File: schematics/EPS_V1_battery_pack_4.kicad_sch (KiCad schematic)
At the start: 31 parts, among them U12 MP2672AGD-0000-Z, U13 MAX17205G+

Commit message: Fix NC pins, add 2 test points & silkscreen labels
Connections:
- net GND: now also U12.14 (SCL), U12.15 (SDA), U13.10 (AIN2), U13.9 (AIN1)
- no-connect marks 6 -> 2
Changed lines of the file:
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@@
+	)
+	(junction
+		(at 104.14 90.17)
+		(diameter 0)
+		(color 0 0 0 0)
 	)
 	(junction
@@
 	)
 	(junction
+		(at 229.87 88.9)
+		(diameter 0)
+		(color 0 0 0 0)
+	)
+	(junction
 		(at 257.81 83.82)
 		(diameter 0)
@@
 	)
 	(junction
+		(at 104.14 92.71)
+		(diameter 0)
+		(color 0 0 0 0)
+	)
+	(junction
 		(at 118.11 105.41)
 		(diameter 0)
@@
 	)
 	(no_connect
-		(at 104.14 90.17)
-	)
-	(no_connect
 		(at 229.87 78.74)
-	)
-	(no_connect
-		(at 229.87 91.44)
 	)
 	(no_connect
 		(at 104.14 95.25)
 	)
-	(no_connect
-		(at 104.14 87.63)
-	)
-	(no_connect
-		(at 229.87 88.9)
-	)
 	(wire
 		(pts
@@
 	(wire
 		(pts
+			(xy 229.87 96.52) (xy 229.87 93.98)
+		)
+		(stroke
+			(width 0)
+			(type default)
+		)
+	)
+	(wire
+		(pts
 			(xy 160.02 78.74) (xy 184.15 78.74)
 		)
@@
 	(wire
 		(pts
-			(xy 229.87 93.98) (xy 231.14 93.98)
+			(xy 229.87 96.52) (xy 232.41 96.52)
 		)
 		(stroke
@@
 	(wire
 		(pts
+			(xy 104.14 90.17) (xy 104.14 92.71)
+		)
+		(stroke
+			(width 0)
+			(type default)
+		)
+	)
+	(wire
+		(pts
 			(xy 114.3 64.77) (xy 48.26 64.77)
 		)
@@
 	(wire
 		(pts
+			(xy 229.87 88.9) (xy 229.87 91.44)
+		)
+		(stroke
+			(width 0)
+			(type default)
+		)
+	)
+	(wire
+		(pts
 			(xy 181.61 83.82) (xy 181.61 102.87)
 		)
@@
 	(wire
 		(pts
+			(xy 104.14 87.63) (xy 104.14 90.17)
+		)
+		(stroke
+			(width 0)
+			(type default)
+		)
+	)
+	(wire
+		(pts
 			(xy 63.5 97.79) (xy 50.8 97.79)
 		)
@@
 		(pts
 			(xy 100.33 107.95) (xy 100.33 120.65)
+		)
+		(stroke
+			(width 0)
+			(type default)
+		)
+	)
+	(wire
+		(pts
+			(xy 229.87 88.9) (xy 233.68 88.9)
 		)
 		(stroke
@@
 	(global_label "ALRT"
 		(shape output)
-		(at 231.14 93.98 0)
+		(at 232.41 96.52 0)
 		(fields_autoplaced yes)
 		(effects
@@
 		)
 		(property "Intersheetrefs" "${INTERSHEET_REFS}"
-			(at 238.4795 93.98 0)
+			(at 239.7495 96.52 0)
 			(hide yes)
 			(show_name no)
@@
 					(unit 1)
 				)
+			)
+		)
+	)
+	(symbol
+		(lib_id "power:GND")
+		(at 233.68 88.9 0)
+		(unit 1)
+		(body_style 1)
+		(exclude_from_sim no)
+		(in_bom yes)
+		(on_board yes)
+		(in_pos_files yes)
+		(dnp no)
+		(property "Reference" "#PWR0129"
+			(at 233.68 95.25 0)
+			(hide yes)
+			(show_name no)
+			(do_not_autoplace no)
+			(effects
+				(font
+					(size 1.27 1.27)
+				)
+			)
+		)
+		(property "Value" "GND"
+			(at 233.68 92.964 0)
+			(show_name no)
+			(do_not_autoplace no)
+			(effects
+				(font
+					(size 1.27 1.27)
+				)
+			)
+		)
+		(property "Footprint" ""
+			(at 233.68 88.9 0)
+			(hide yes)
+			(show_name no)
+			(do_not_autoplace no)
+			(effects
+				(font
+					(size 1.27 1.27)
+				)
+			)
+		)
+		(property "Datasheet" ""
+			(at 233.68 88.9 0)
+			(hide yes)
+			(show_name no)
+			(do_not_autoplace no)
+			(effects
+				(font
+					(size 1.27 1.27)
+				)
+			)
+		)
+		(property "Description" "Power symbol creates a global label with name \"GND\" , ground"
+			(at 233.68 88.9 0)
+			(hide yes)
+			(show_name no)
+			(do_not_autoplace no)
+			(effects
+				(font
+					(size 1.27 1.27)
+				)
+			)
+		)
+		(pin "1"
+		)
+		(instances
+			(project "EPS_V1"
+				(path "/85157432-5d03-48fa-ab40-27ed3d133f47/5659a67b-3108-4102-8b7c-09d96e8fb3f7"
+					(reference "#PWR0129")
+					(unit 1)
+				)

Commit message: Fix silkscreen; Fix component value style
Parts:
- C_BATT8, C_BST4: value 0.1u -> 100n
- C_REG8, C_REG9: value 0.47u -> 470n
- R_BATT4, R_MID4: value 50 -> 50R
- R_SCL4, R_SDA4: value 150 -> 150R
- R_SENSE4: value 0.01 -> 10m
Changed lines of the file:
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@@
 			)
 		)
-		(property "Value" "0.01"
+		(property "Value" "10m"
 			(at 201.676 108.204 90)
 			(show_name no)
@@
 			)
 		)
-		(property "Value" "50"
+		(property "Value" "50R"
 			(at 165.354 81.534 90)
 			(show_name no)
@@
 			)
 		)
-		(property "Value" "0.1u"
+		(property "Value" "100n"
 			(at 167.132 88.9 0)
 			(show_name no)
@@
 			)
 		)
-		(property "Value" "0.47u"
+		(property "Value" "470n"
 			(at 172.212 101.6 0)
 			(show_name no)
@@
 			)
 		)
-		(property "Value" "150"
+		(property "Value" "150R"
 			(at 247.904 91.186 90)
 			(show_name no)
@@
 			)
 		)
-		(property "Value" "50"
+		(property "Value" "50R"
 			(at 61.722 102.87 0)
 			(show_name no)
@@
 			)
 		)
-		(property "Value" "0.47u"
+		(property "Value" "470n"
 			(at 182.118 116.84 0)
 			(show_name no)
@@
 			)
 		)
-		(property "Value" "150"
+		(property "Value" "150R"
 			(at 263.144 78.994 90)
 			(show_name no)
@@
 			)
 		)
-		(property "Value" "0.1u"
+		(property "Value" "100n"
 			(at 55.118 80.01 0)
 			(show_name no)

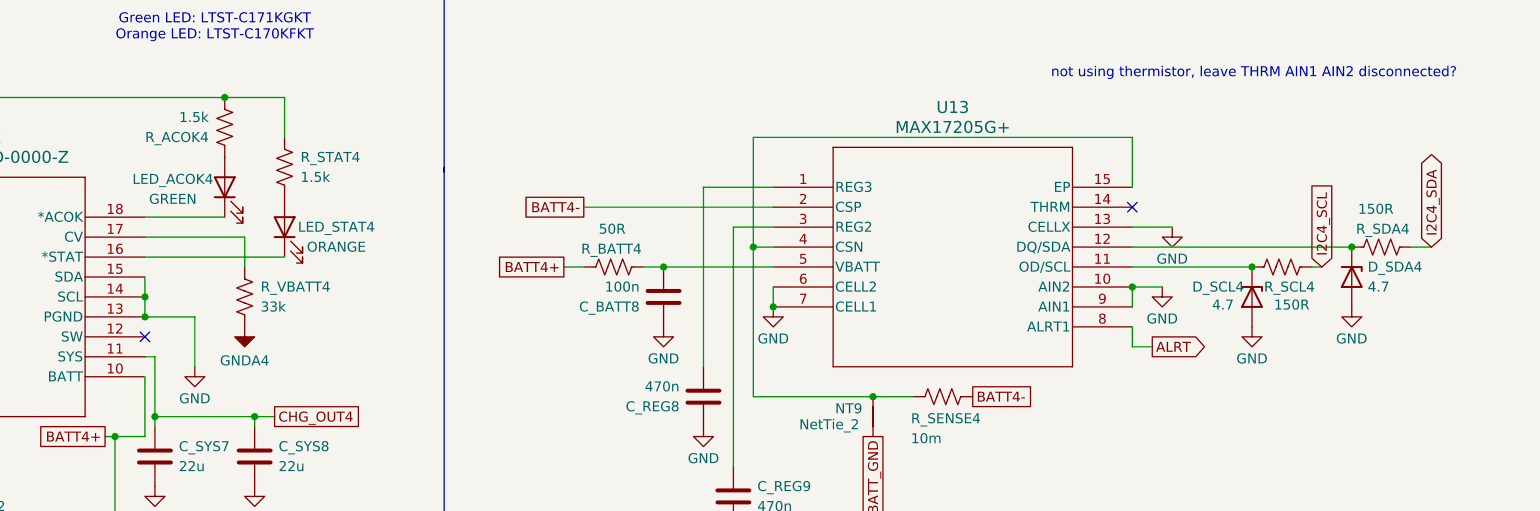
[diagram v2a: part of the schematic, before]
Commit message: Add chargers to I2C, chg_in for ADC
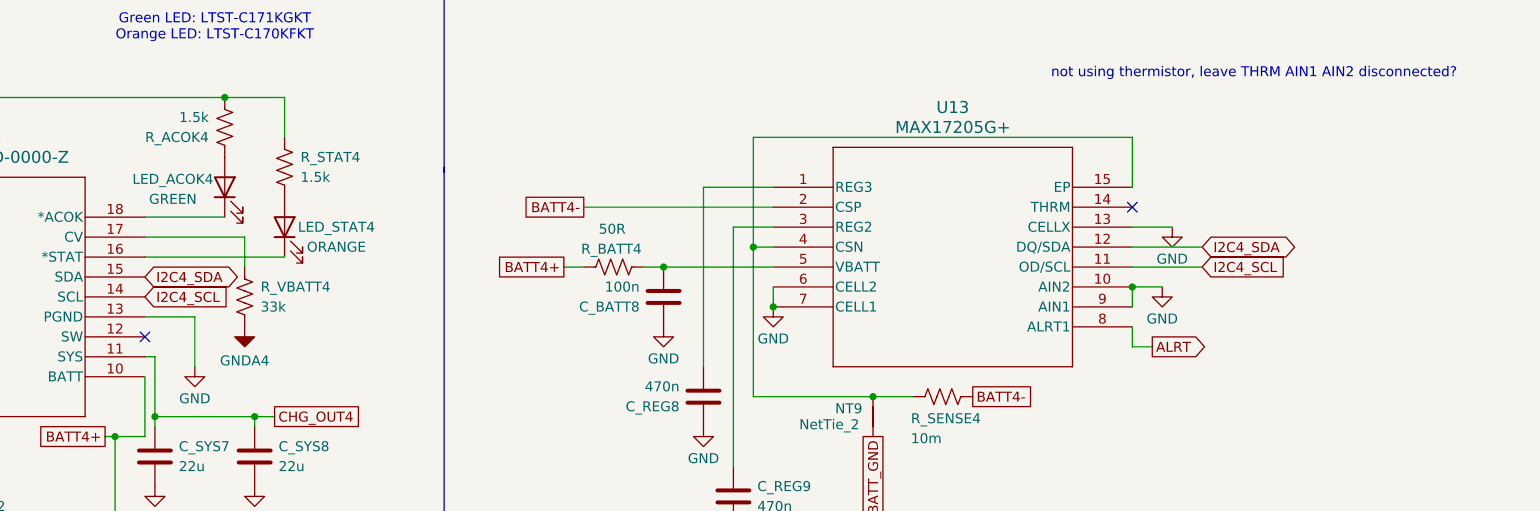
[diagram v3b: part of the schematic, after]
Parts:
- removed D_SCL4, D_SDA4: 4.7, Diode_SMD:D_0603_1608Metric, symbol Device:D_Zener
- removed R_SCL4, R_SDA4: 150R, Resistor_SMD:R_0603_1608Metric, symbol Device:R_US
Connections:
- net GND: no longer U12.14 (SCL), U12.15 (SDA)
- net I2C4_SCL: now also U12.14 (SCL), U13.11 (OD/SCL)
- net I2C4_SDA: now also U12.15 (SDA), U13.12 (DQ/SDA)

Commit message: Fix standalone to host control mode
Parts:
- removed R_VBATT4: 33k, Resistor_SMD:R_0603_1608Metric, symbol Device:R_US
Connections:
- net at C_VCC4.2, R_ACOK4.2, R_STAT4.1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: now also U12.17 (CV)
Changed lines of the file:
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@@
 	)
 	(junction
+		(at 105.41 64.77)
+		(diameter 0)
+		(color 0 0 0 0)
+	)
+	(junction
 		(at 58.42 77.47)
 		(diameter 0)
@@
 	(wire
 		(pts
+			(xy 105.41 64.77) (xy 48.26 64.77)
+		)
+		(stroke
+			(width 0)
+			(type default)
+		)
+	)
+	(wire
+		(pts
 			(xy 41.91 100.33) (xy 41.91 87.63)
 		)
@@
 	(wire
 		(pts
-			(xy 114.3 64.77) (xy 48.26 64.77)
+			(xy 114.3 64.77) (xy 105.41 64.77)
 		)
 		(stroke
@@
 	(wire
 		(pts
-			(xy 116.84 82.55) (xy 116.84 86.36)
+			(xy 104.14 82.55) (xy 105.41 82.55)
 		)
 		(stroke
@@
 	(wire
 		(pts
-			(xy 104.14 82.55) (xy 116.84 82.55)
-		)
-		(stroke
-			(width 0)
-			(type default)
-		)
-	)
-	(wire
-		(pts
 			(xy 45.72 107.95) (xy 41.91 107.95)
 		)
@@
 	(wire
 		(pts
+			(xy 105.41 82.55) (xy 105.41 64.77)
+		)
+		(stroke
+			(width 0)
+			(type default)
+		)
+	)
+	(wire
+		(pts
 			(xy 99.06 107.95) (xy 100.33 107.95)
 		)
@@
 	)
 	(symbol
-		(lib_id "Device:R_US")
-		(at 116.84 90.17 0)
-		(unit 1)
-		(body_style 1)
-		(exclude_from_sim no)
-		(in_bom yes)
-		(on_board yes)
-		(in_pos_files yes)
-		(dnp no)
-		(property "Reference" "R_VBATT4"
-			(at 118.872 88.9 0)
-			(show_name no)
-			(do_not_autoplace no)
-			(effects
-				(font
-					(size 1.27 1.27)
-				)
-				(justify left)
-			)
-		)
-		(property "Value" "33k"
-			(at 118.872 91.44 0)
-			(show_name no)
-			(do_not_autoplace no)
-			(effects
-				(font
-					(size 1.27 1.27)
-				)
-				(justify left)
-			)
-		)
-		(property "Footprint" "Resistor_SMD:R_0603_1608Metric"
-			(at 117.856 90.424 90)
-			(hide yes)
-			(show_name no)
-			(do_not_autoplace no)
-			(effects
-				(font
-					(size 1.27 1.27)
-				)
-			)
-		)
-		(property "Datasheet" ""
-			(at 116.84 90.17 0)
-			(hide yes)
-			(show_name no)
-			(do_not_autoplace no)
-			(effects
-				(font
-					(size 1.27 1.27)
-				)
-			)
-		)
-		(property "Description" "Resistor, US symbol"
-			(at 116.84 90.17 0)
-			(hide yes)
-			(show_name no)
-			(do_not_autoplace no)
-			(effects
-				(font
-					(size 1.27 1.27)
-				)
-			)
-		)
-		(pin "2"
-		)
-		(pin "1"
-		)
-		(instances
-			(project "EPS_V1"
-				(path "/85157432-5d03-48fa-ab40-27ed3d133f47/5659a67b-3108-4102-8b7c-09d96e8fb3f7"
-					(reference "R_VBATT4")
-					(unit 1)
-				)
-			)
-		)
-	)
-	(symbol
 		(lib_id "power:GND")
 		(at 234.95 81.28 0)
@@
 					(unit 1)
 				)
-			)
-		)
-	)
-	(symbol
-		(lib_id "sym_lib:GNDA4")
-		(at 116.84 93.98 0)
-		(unit 1)
-		(body_style 1)
-		(exclude_from_sim no)
-		(in_bom yes)
-		(on_board yes)
-		(in_pos_files yes)
-		(dnp no)
-		(property "Reference" "#PWR094"
-			(at 116.84 93.98 0)
-			(hide yes)
-			(show_name no)
-			(do_not_autoplace no)
-			(effects
-				(font
-					(size 1.27 1.27)
-				)
-			)
-		)
-		(property "Value" "GNDA4"
-			(at 116.84 98.298 0)
-			(show_name no)
-			(do_not_autoplace no)
-			(effects
-				(font
-					(size 1.27 1.27)
-				)
-			)
-		)
-		(property "Footprint" ""
-			(at 116.84 93.98 0)
-			(hide yes)
-			(show_name no)
-			(do_not_autoplace no)
-			(effects
-				(font
-					(size 1.27 1.27)
-				)
-			)
-		)
-		(property "Datasheet" ""
-			(at 116.84 93.98 0)
-			(hide yes)
-			(show_name no)
-			(do_not_autoplace no)
-			(effects
-				(font
-					(size 1.27 1.27)
-				)
-			)
-		)
-		(property "Description" ""
-			(at 116.84 93.98 0)
-			(hide yes)
-			(show_name no)
-			(do_not_autoplace no)
-			(effects
-				(font
-					(size 1.27 1.27)
-				)
-			)
-		)
-		(pin "1"
-		)
-		(instances
-			(project "EPS_V1"
-				(path "/85157432-5d03-48fa-ab40-27ed3d133f47/5659a67b-3108-4102-8b7c-09d96e8fb3f7"
-					(reference "#PWR094")
-					(unit 1)
-				)

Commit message: fix U6 EN pin, add ALRT pullup R, update 3dmodels, regen step
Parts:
- R_ISET4: value 6k -> 24k
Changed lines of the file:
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@@
 			)
 		)
-		(property "Value" "6k"
+		(property "Value" "24k"
 			(at 48.768 130.81 0)
 			(show_name no)
